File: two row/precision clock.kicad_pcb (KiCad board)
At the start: 2 copper layers, 170 x 60 mm, 41 parts, among them J2 Barrel_Jack_Switch, Q1 2N5401, Q2 2N5401

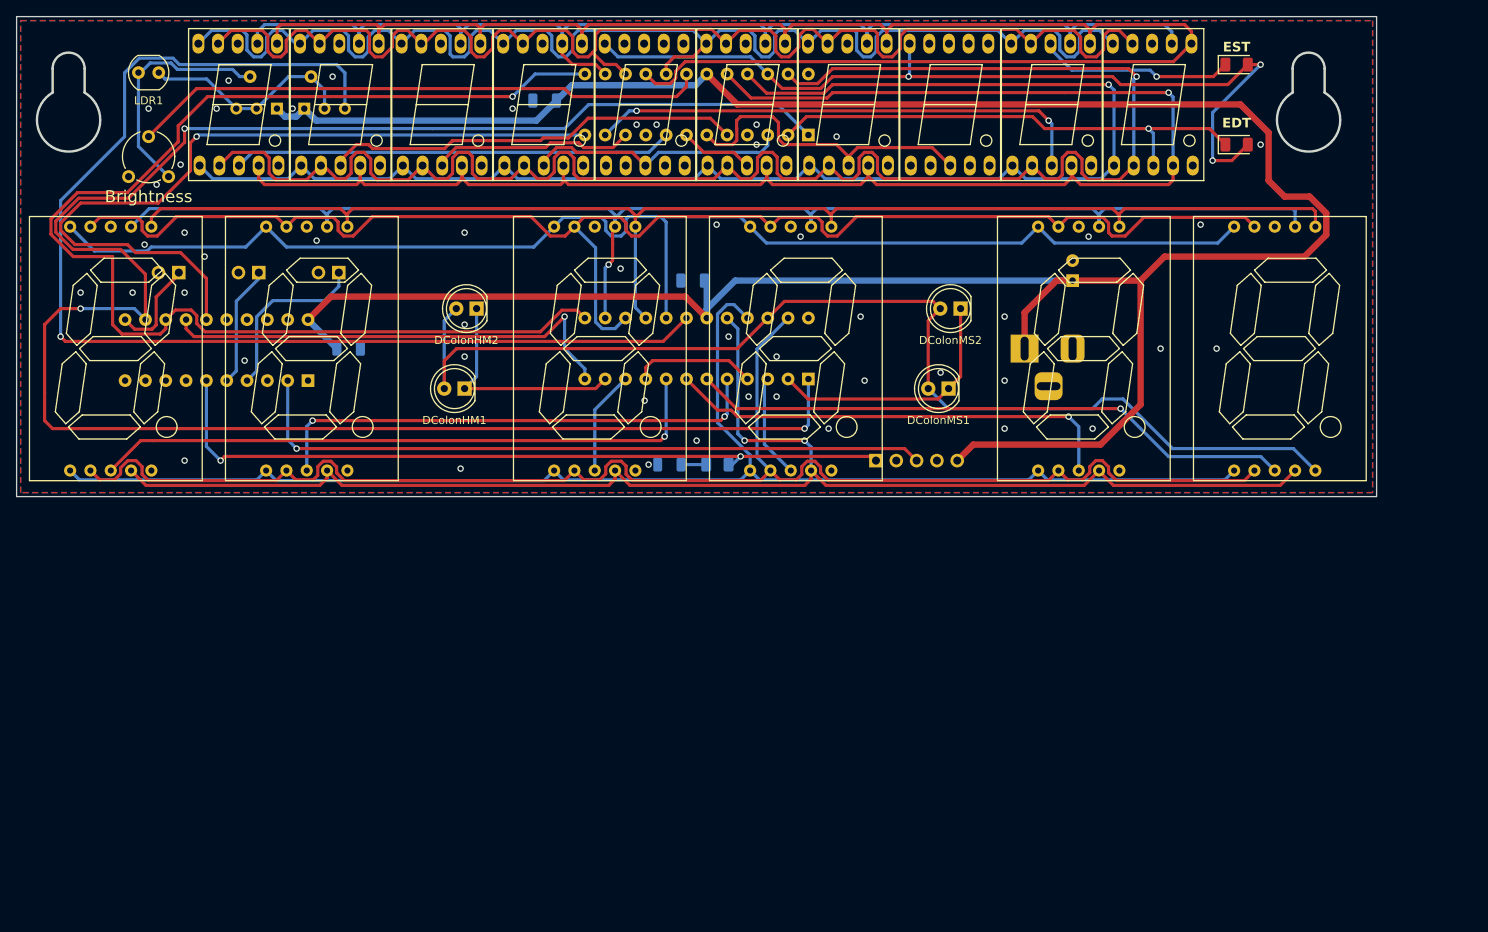
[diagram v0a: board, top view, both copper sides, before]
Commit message: Rebuild two-row for 0.8" segments and improvements from prototype (1.0" are very difficult to source)
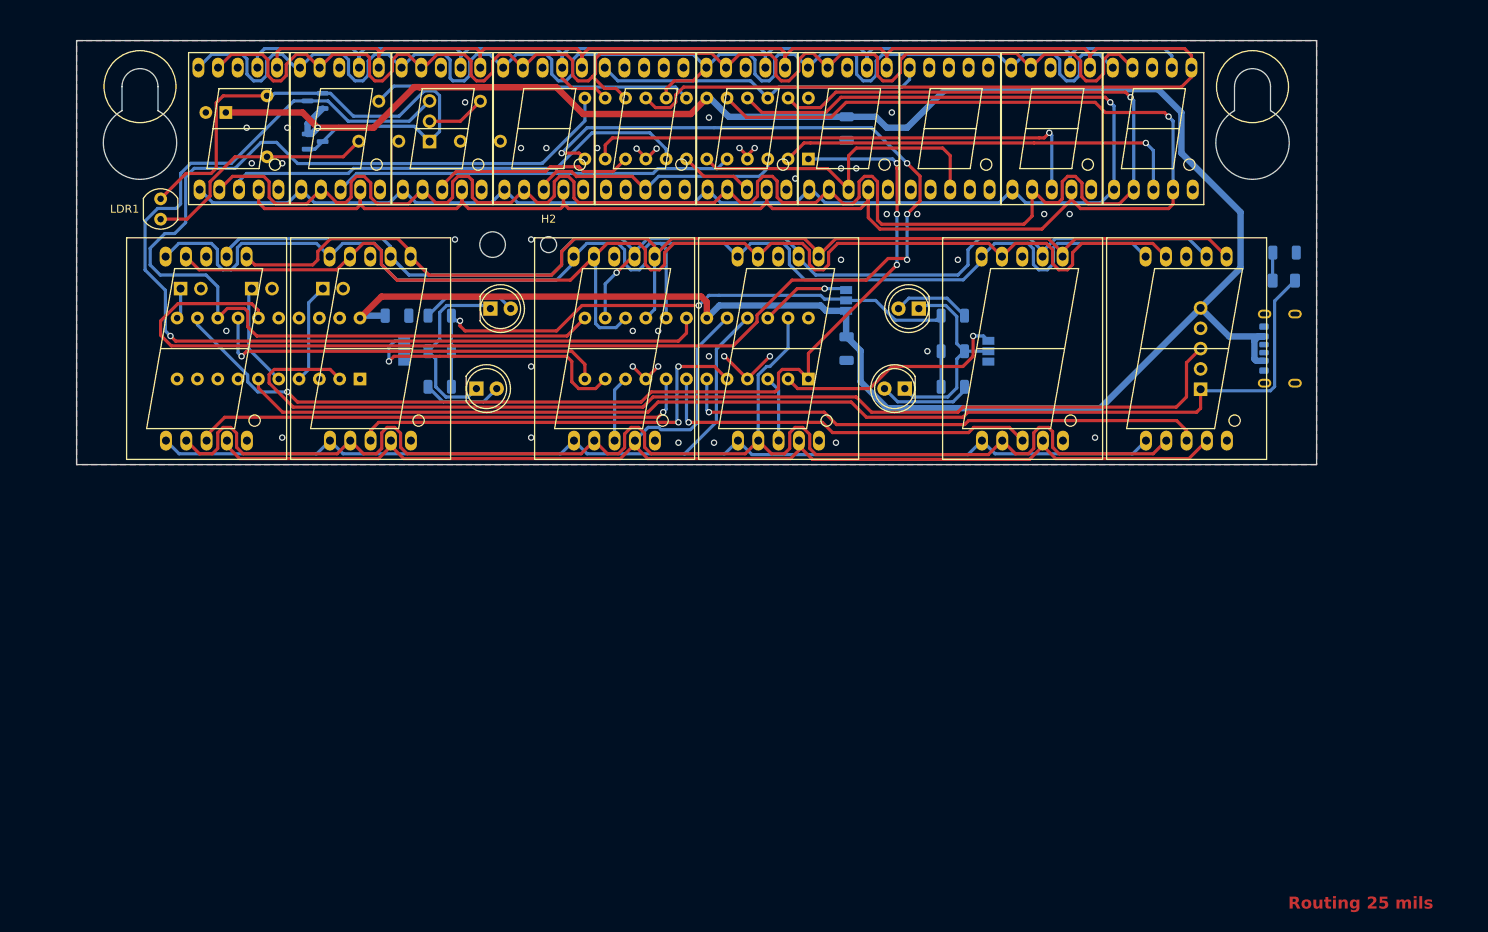
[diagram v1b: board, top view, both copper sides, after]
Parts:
- removed C5: 0.1uF, Capacitor_SMD:C_1206_3216Metric
- removed D_BST1, D_GMT1: LED, LED_SMD:LED_1206_3216Metric
- removed J2: Barrel_Jack_Switch, Connector_BarrelJack:BarrelJack_Horizontal
- added C2: 0.1uF, Capacitor_SMD:C_1206_3216Metric, B.Cu at (123.2, 100.0)
- added H1: MountingHole, MountingHole:MountingHole_3.2mm_M3, F.Cu at (79.0, 87.0)
- added H2: MountingHole, MountingHole:MountingHole_2mm, F.Cu at (86.0, 87.0)
- added JP4: Time_brt_mode, Connector_PinHeader_2.54mm:PinHeader_1x03_P2.54mm_Vertical, B.Cu at (71.1, 74.1)
- added JP5: UTC, Connector_PinHeader_2.54mm:PinHeader_1x02_P2.54mm_Vertical, B.Cu at (57.8, 92.5)
- added JP6: Perm_DST, Connector_PinHeader_2.54mm:PinHeader_1x02_P2.54mm_Vertical, B.Cu at (48.9, 92.5)
- added JP7: DST, Connector_PinHeader_2.54mm:PinHeader_1x02_P2.54mm_Vertical, B.Cu at (40.0, 92.5)
- added P1: USB_C_Plug_USB2.0, Connector_USB:USB_C_Receptacle_GCT_USB4125-xx-x_6P_TopMnt_Horizontal, B.Cu at (178.5, 100.0)
- added R1: 330, Resistor_SMD:R_1206_3216Metric, B.Cu at (72.4, 104.8)
- added R2: 330, Resistor_SMD:R_1206_3216Metric, B.Cu at (72.4, 95.9)
- added R3: 150, Resistor_SMD:R_1206_3216Metric, B.Cu at (72.4, 100.3)
- added R4: 330, Resistor_SMD:R_1206_3216Metric, B.Cu at (136.5, 104.8)
- added R5: 330, Resistor_SMD:R_1206_3216Metric, B.Cu at (136.5, 95.9)
- added R6: 150, Resistor_SMD:R_1206_3216Metric, B.Cu at (136.5, 100.3)
- added R_Time_brt_adj1: 100K, Potentiometer_THT:Potentiometer_Piher_PT-6-V_Vertical, B.Cu at (75.0, 74.1)
- C1: value 100uF -> C_Polarized_Small_US
- DHr1, DMin1, DSec1, DTenHr1, DTenMin1, DTenSec1: footprint precision clock:7seg1inchCC -> precision clock:7seg0.8CC
- JP1: value Jumper_2_Open -> HM src; footprint Connector_PinHeader_2.54mm:PinHeader_1x02_P2.54mm_Vertical -> Jumper:SolderJumper-3_P1.3mm_Open_Pad1.0x1.5mm
- JP2: value Jumper_2_Open -> HM/MS mode; footprint Connector_PinHeader_2.54mm:PinHeader_1x02_P2.54mm_Vertical -> Jumper:SolderJumper-3_P1.3mm_Open_Pad1.0x1.5mm
- JP3: value Jumper_2_Open -> MS src; footprint Connector_PinHeader_2.54mm:PinHeader_1x02_P2.54mm_Vertical -> Jumper:SolderJumper-3_P1.3mm_Open_Pad1.0x1.5mm
- Q1, Q2: value 2N5401 -> MMBT3906; footprint Package_TO_SOT_THT:TO-92_Inline_Wide -> Package_TO_SOT_SMD:SOT-23
- R_Max_Bright1: value 50K -> 100K; moved to B.Cu
- U_GPS1: footprint Connector_PinHeader_2.54mm:PinHeader_1x05_P2.54mm_Vertical -> Connector_PinSocket_2.54mm:PinSocket_1x05_P2.54mm_Horizontal
- moved C1 107.9 mm to (45.7, 70.5), turned to 180 degrees
- moved JP3 81.8 mm to (141.0, 100.3)
- moved R_PPS1 81.3 mm to (178.0, 88.0), turned to 0 degrees
- moved D_PPS1 74.4 mm to (177.9, 91.5)
- moved JP2 73.5 mm to (123.2, 94.0)
- moved U_GPS1 41.5 mm to (167.5, 105.1), turned to 0 degrees
- moved JP1 29.8 mm to (67.9, 100.3)
- moved C3 27.0 mm to (123.2, 72.5), turned to -90 degrees
- moved R_Max_Bright1 24.2 mm to (62.3, 74.1)
- moved LDR1 15.8 mm to (37.5, 81.3), turned to -90 degrees
- moved DTenHr1 13.2 mm to (43.2, 100.0)
- moved DSec1 9.75 mm to (165.8, 100.0)
- moved DHr1 9.25 mm to (63.8, 100.0)
- moved C4 7.32 mm to (67.1, 95.9), turned to 180 degrees
- moved U_CONTROL1 6.50 mm to (62.4, 103.8)
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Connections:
- C3 pad 1: GND -> +5V
- C3 pad 2: +5V -> GND
- C4 pad 1: +5V -> GND
- C4 pad 2: GND -> +5V
- DColonHM1 pad 2: /timeDP -> Net-(DColonHM1-A)
- DColonHM2 pad 2: /timeDP -> Net-(DColonHM2-A)
- DColonMS1 pad 2: /timeDP -> Net-(DColonMS1-A)
- DColonMS2 pad 2: /timeDP -> Net-(DColonMS2-A)
- DSec1 pad 5: /timeDP -> unconnected-(DSec1-DP-Pad5)
- DTenDay1 pad 8: Net-(D_GMT1-K) -> unconnected-(DTenDay1-CC-Pad8)
- JP1 pad 1: /DST_EN* -> GND
- JP1 pad 2: GND -> Net-(DColonHM1-K)
- JP2 pad 1: Net-(JP2-A) -> +5V
- JP2 pad 2: GND -> Net-(JP2-C)
- JP3 pad 1: Net-(JP3-A) -> GND
- JP3 pad 2: GND -> Net-(DColonMS1-K)
- LDR1 pad 1: Net-(Q1-B) -> Net-(JP4-A)
- Q1 pad 1: +5V -> Net-(JP4-A)
- Q1 pad 2: Net-(Q1-B) -> +5V
- Q1 pad 3: Net-(Q1-B) -> Net-(JP4-A)
- Q2 pad 1: +5V -> Net-(JP4-A)
- Q2 pad 2: Net-(Q1-B) -> +5V
- R_Min_Bright1 pad 1: Net-(Q1-B) -> Net-(JP4-A)
- UTimeDrv1 pad 11: Net-(DColonHM1-K) -> Net-(JP1-B)
- UTimeDrv1 pad 2: Net-(DColonMS1-K) -> Net-(JP3-B)
- U_CONTROL1 pad 4: Net-(JP3-A) -> Net-(JP5-A)
- U_CONTROL1 pad 5: Net-(JP2-A) -> Net-(JP6-A)
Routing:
- net /timeDP: track 143.8 -> 11.4 mm, vias 0 -> 1
- net /SPI_DATA: track 251.0 -> 127.9 mm, vias 3 -> 4
- net Net-(JP2-C): track 0.00 -> 83.5 mm, vias 0 -> 2
- net /LD_DATE: track 98.9 -> 178.1 mm, vias 1 -> 4
- net Net-(JP4-A): track 0.00 -> 71.3 mm
- net /dateDP: track 110.2 -> 42.1 mm, vias 3 -> 0
- net Net-(D_PPS1-A): track 95.0 -> 148.2 mm, vias 2 -> 0
- net /GPS_DATA: track 87.1 -> 135.4 mm, vias 1 -> 0
- net +5V: track 346.4 -> 305.8 mm, vias 0 -> 1
- net Net-(JP1-B): track 0.00 -> 35.0 mm, vias 0 -> 1
- net /ISET_DATE: track 72.2 -> 39.9 mm
- net Net-(JP3-B): track 0.00 -> 30.0 mm, vias 0 -> 1
- net /timeB: track 175.4 -> 146.5 mm
- net Net-(Q1-B): track 27.3 -> 0.00 mm
- net /timeE: track 176.6 -> 149.6 mm
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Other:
- board size 170 x 60 mm -> 155 x 53 mm
- board text added: "+"
- board text added: "-"
- board text added: "1-2 : Constant 2-3 : MAX7219"
- board text added: "Ant. mount"
- board text added: "JP 1,2,3 Colon mode"
- board text added: "Overall"
- board text added: "Part DST"
- board text added: "Relative"
- board text added: "Routing 25 mils"
- board text removed: "5V"
- board text removed: "Brightness"
- board text removed: "DST"
- board text removed: "EDT"
- board text removed: "EST"

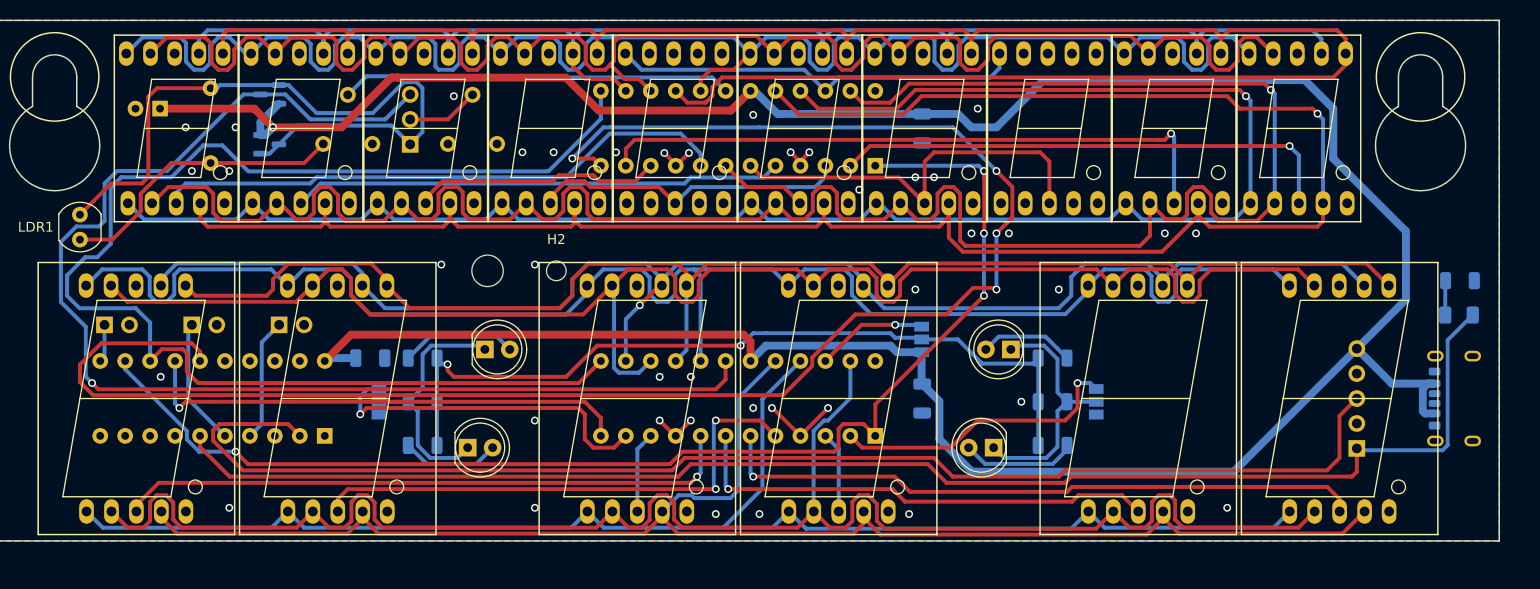
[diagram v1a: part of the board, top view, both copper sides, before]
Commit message: Remove extra resistors, add second USB port location, cleanup trace routing
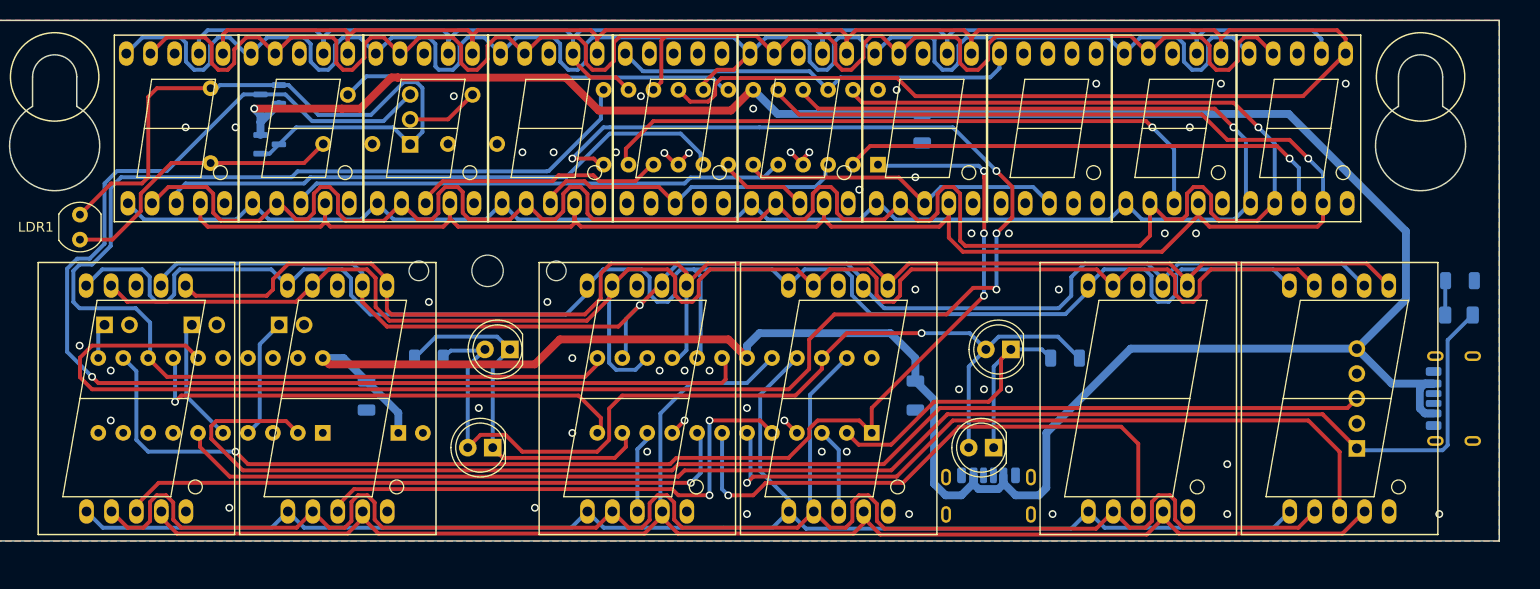
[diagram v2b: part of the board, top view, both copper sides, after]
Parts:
- removed JP1: HM src, Jumper:SolderJumper-3_P1.3mm_Open_Pad1.0x1.5mm
- removed JP2: HM/MS mode, Jumper:SolderJumper-3_P1.3mm_Open_Pad1.0x1.5mm
- removed JP3: MS src, Jumper:SolderJumper-3_P1.3mm_Open_Pad1.0x1.5mm
- removed R1, R2, R4, R5: 330, Resistor_SMD:R_1206_3216Metric
- added H3: MountingHole, MountingHole:MountingHole_2mm, F.Cu at (72.0, 87.0)
- added P2: USB_C_Plug_USB2.0, Connector_USB:USB_C_Receptacle_HRO_TYPE-C-31-M-17, B.Cu at (130.0, 111.0)
- P1: footprint Connector_USB:USB_C_Receptacle_GCT_USB4125-xx-x_6P_TopMnt_Horizontal -> Connector_USB:USB_C_Receptacle_HRO_TYPE-C-31-M-17
- moved C1 41.0 mm to (69.9, 103.5), turned to 0 degrees
- moved R6 4.62 mm to (137.8, 95.9), turned to 0 degrees
- moved R3 4.49 mm to (73.0, 95.9)
- moved C4 3.83 mm to (66.7, 99.7), turned to 90 degrees
- moved DColonHM1 2.55 mm to (79.5, 105.0), turned to 180 degrees
- moved DColonHM2 2.55 mm to (81.3, 95.0), turned to 180 degrees
- moved C2 0.76 mm to (122.6, 99.7)
- moved UTimeDrv1 0.47 mm to (118.1, 103.5)
- moved U_CONTROL1 0.36 mm to (62.2, 103.5)
- moved UDateDrv1 0.30 mm to (118.8, 76.2)
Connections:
- DColonHM1 pad 2: Net-(DColonHM1-A) -> /timeDP
- DColonHM2 pad 2: Net-(DColonHM2-A) -> /timeDP
- DColonMS1 pad 2: Net-(DColonMS1-A) -> /timeDP
- DColonMS2 pad 2: Net-(DColonMS2-A) -> /timeDP
- R3 pad 2: Net-(JP2-C) -> /timeDP
- R6 pad 2: Net-(JP2-C) -> /timeDP
- UTimeDrv1 pad 11: Net-(JP1-B) -> Net-(DColonHM1-K)
- UTimeDrv1 pad 2: Net-(JP3-B) -> Net-(DColonMS1-K)
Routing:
- net /timeDP: track 11.4 -> 99.2 mm
- net Net-(JP2-C): track 83.5 -> 0.00 mm, vias 2 -> 0
- net Net-(JP1-B): track 35.0 -> 0.00 mm, vias 1 -> 0
- net Net-(JP3-B): track 30.0 -> 0.00 mm, vias 1 -> 0
- net Net-(DColonMS1-K): track 25.6 -> 38.2 mm
- net Net-(DColonHM2-A): track 11.8 -> 0.00 mm
- net Net-(DColonMS1-A): track 11.7 -> 0.00 mm
- net Net-(DColonHM1-K): track 26.2 -> 37.5 mm
- net Net-(UTimeDrv1-DIG_3): track 48.8 -> 58.9 mm
- net Net-(DColonHM1-A): track 10.0 -> 0.00 mm
- net Net-(DColonMS2-A): track 9.70 -> 0.00 mm
- net GND: track 21.0 -> 12.0 mm, vias 41 -> 53
- net Net-(UTimeDrv1-DIG_2): track 66.6 -> 75.3 mm
- net Net-(UDateDrv1-DIG_2): track 41.3 -> 33.4 mm
- net /SPI_CLK: track 134.8 -> 129.8 mm
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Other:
- board text removed: "1-2 : Constant 2-3 : MAX7219"
- board text removed: "JP 1,2,3 Colon mode"

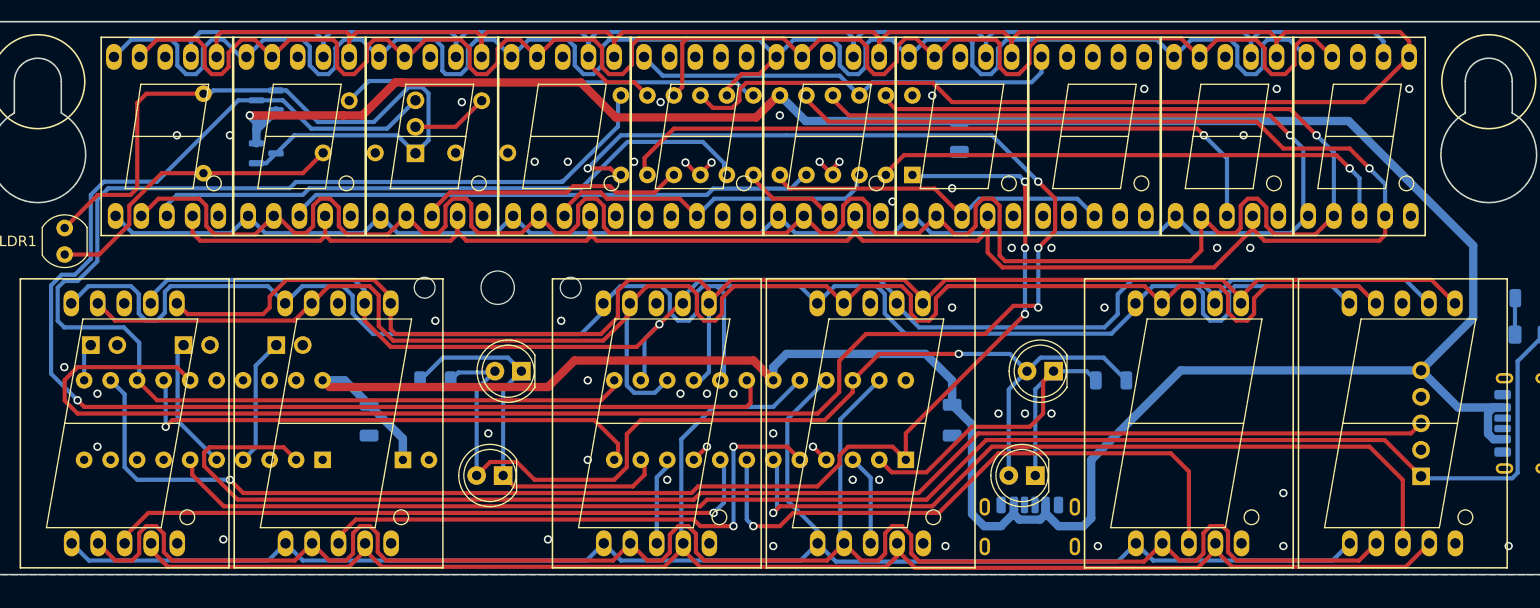
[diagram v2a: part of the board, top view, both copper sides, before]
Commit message: Add wire to seconds decimal point
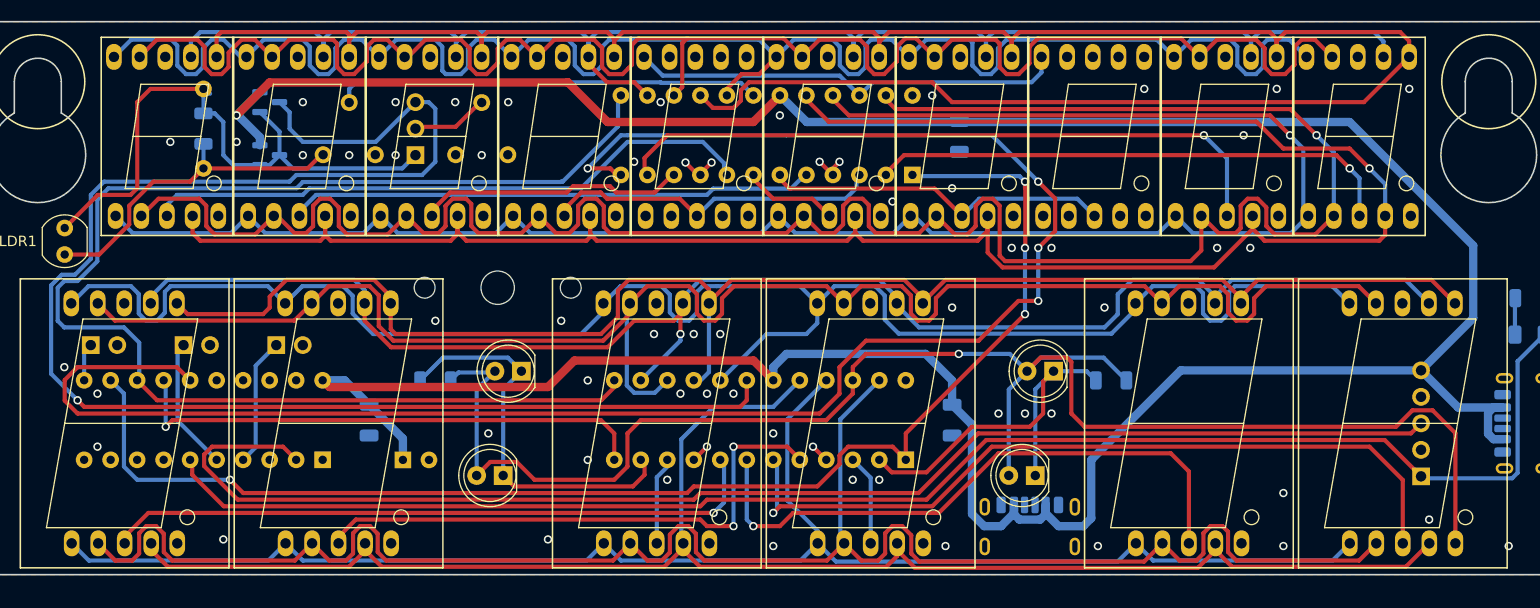
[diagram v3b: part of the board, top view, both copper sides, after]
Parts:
- added R_Min_Bright2: 10M, Resistor_SMD:R_1206_3216Metric, B.Cu at (50.8, 71.8)
- moved R_Min_Bright1 0.46 mm to (50.8, 67.9)
- moved Q1 0.38 mm to (57.1, 74.3)
- moved Q2 0.38 mm to (57.1, 69.2), turned to 0 degrees
- moved JP4 0.17 mm to (71.1, 74.3)
- moved R_Max_Bright1 0.17 mm to (62.3, 74.3)
- moved R_Time_brt_adj1 0.17 mm to (75.0, 74.3)
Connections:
- DSec1 pad 5: unconnected-(DSec1-DP-Pad5) -> /timeDP
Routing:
- net /timeDP: track 99.2 -> 159.4 mm
- net /ISET_TIME: track 127.0 -> 148.3 mm
- net Net-(JP4-A): track 71.3 -> 57.2 mm
- net /timeG: track 161.7 -> 165.8 mm
- net +5V: track 309.6 -> 313.0 mm
- net /timeA: track 145.7 -> 149.0 mm
- net Net-(LDR1-Pad2): track 29.9 -> 32.2 mm
- net /ISET_DATE: track 39.9 -> 40.7 mm
- net /LD_DATE: track 177.9 -> 177.1 mm
- net Net-(UDateDrv1-DIG_1): track 65.4 -> 64.9 mm
- net GND: vias 53 -> 62
